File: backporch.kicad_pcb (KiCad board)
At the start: 2 copper layers, 53.3 x 32.4 mm, 31 parts, among them J1 MD-90SM, J2 MD-80SM, J3 DB15_Female_HighDensity_Mount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, J4 35RAPC4BH3, U1 EL1883ISZ

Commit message: PCB: add space between signal traces
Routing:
- net GREEN_75: track 49.7 -> 52.3 mm
- net Net-(C6-Pad1): track 39.5 -> 40.1 mm
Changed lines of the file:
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@@
     (thickness 1.6)
     (drawings 7)
-    (tracks 227)
+    (tracks 229)
     (zones 0)
     (modules 31)
@@
   (segment (start 114.935 92.51) (end 114.935 91.44) (width 0.25) (layer B.Cu) (net 8) (status 10))
   (segment (start 135.475 79.375) (end 136.525 79.375) (width 0.25) (layer F.Cu) (net 8) (status 20))
-  (segment (start 112.395 88.9) (end 112.395 83.114732) (width 0.25) (layer F.Cu) (net 8))
   (segment (start 112.395 83.114732) (end 116.519742 78.98999) (width 0.25) (layer F.Cu) (net 8))
   (segment (start 116.519742 78.98999) (end 126.240832 78.98999) (width 0.25) (layer F.Cu) (net 8))
-  (segment (start 134.349999 80.500001) (end 135.475 79.375) (width 0.25) (layer F.Cu) (net 8))
-  (segment (start 126.240832 78.98999) (end 127.750843 80.500001) (width 0.25) (layer F.Cu) (net 8))
-  (segment (start 127.750843 80.500001) (end 134.349999 80.500001) (width 0.25) (layer F.Cu) (net 8))
+  (segment (start 112.395 88.9) (end 112.395 83.114732) (width 0.25) (layer F.Cu) (net 8))
+  (segment (start 126.240832 78.98999) (end 128.530842 81.28) (width 0.25) (layer F.Cu) (net 8))
+  (segment (start 128.530842 81.28) (end 133.57 81.28) (width 0.25) (layer F.Cu) (net 8))
+  (segment (start 133.57 81.28) (end 135.475 79.375) (width 0.25) (layer F.Cu) (net 8))
   (segment (start 138.6475 79.1175) (end 138.39 79.375) (width 0.25) (layer B.Cu) (net 9) (status 30))
   (segment (start 138.865 78.9) (end 138.39 79.375) (width 0.25) (layer B.Cu) (net 9) (status 30))
   (segment (start 139.065 79.335) (end 139.025 79.375) (width 0.25) (layer B.Cu) (net 9) (status 30))
   (segment (start 139.065 77.47) (end 139.065 79.335) (width 0.25) (layer B.Cu) (net 9) (status 30))
-  (segment (start 127.779999 86.442999) (end 133.722997 80.500001) (width 0.25) (layer B.Cu) (net 9))
-  (segment (start 137.899999 80.500001) (end 139.025 79.375) (width 0.25) (layer B.Cu) (net 9) (status 20))
-  (segment (start 127.779999 88.120001) (end 127.779999 86.442999) (width 0.25) (layer B.Cu) (net 9))
-  (segment (start 125.32749 90.57251) (end 127.779999 88.120001) (width 0.25) (layer B.Cu) (net 9))
-  (segment (start 133.722997 80.500001) (end 137.899999 80.500001) (width 0.25) (layer B.Cu) (net 9))
-  (segment (start 119.4168 90.57251) (end 125.32749 90.57251) (width 0.25) (layer B.Cu) (net 9))
-  (segment (start 117.21 92.77931) (end 119.4168 90.57251) (width 0.25) (layer B.Cu) (net 9))
-  (segment (start 117.21 96.665) (end 117.21 92.77931) (width 0.25) (layer B.Cu) (net 9) (status 10))
   (segment (start 148.17363 89.655) (end 148.59 89.655) (width 0.25) (layer F.Cu) (net 9) (status 30))
   (segment (start 139.025 80.50637) (end 148.17363 89.655) (width 0.25) (layer F.Cu) (net 9) (status 20))
   (segment (start 139.025 79.375) (end 139.025 80.50637) (width 0.25) (layer F.Cu) (net 9) (status 10))
+  (segment (start 117.21 91.705) (end 117.21 96.665) (width 0.25) (layer B.Cu) (net 9) (status 20))
+  (segment (start 118.11 90.805) (end 117.21 91.705) (width 0.25) (layer B.Cu) (net 9))
+  (segment (start 126.365 85.725) (end 126.365 90.805) (width 0.25) (layer B.Cu) (net 9))
+  (segment (start 126.365 90.805) (end 118.11 90.805) (width 0.25) (layer B.Cu) (net 9))
+  (segment (start 137.899999 80.500001) (end 137.899999 80.540001) (width 0.25) (layer B.Cu) (net 9))
+  (segment (start 137.899999 80.540001) (end 135.89 82.55) (width 0.25) (layer B.Cu) (net 9))
+  (segment (start 139.025 79.375) (end 137.899999 80.500001) (width 0.25) (layer B.Cu) (net 9) (status 10))
+  (segment (start 131.445 82.55) (end 128.27 85.725) (width 0.25) (layer B.Cu) (net 9))
+  (segment (start 135.89 82.55) (end 131.445 82.55) (width 0.25) (layer B.Cu) (net 9))
+  (segment (start 128.27 85.725) (end 126.365 85.725) (width 0.25) (layer B.Cu) (net 9))
   (via (at 139.7 83.82) (size 0.8) (drill 0.4) (layers F.Cu B.Cu) (net 10))
   (via (at 127 95.25) (size 0.8) (drill 0.4) (layers F.Cu B.Cu) (net 10))

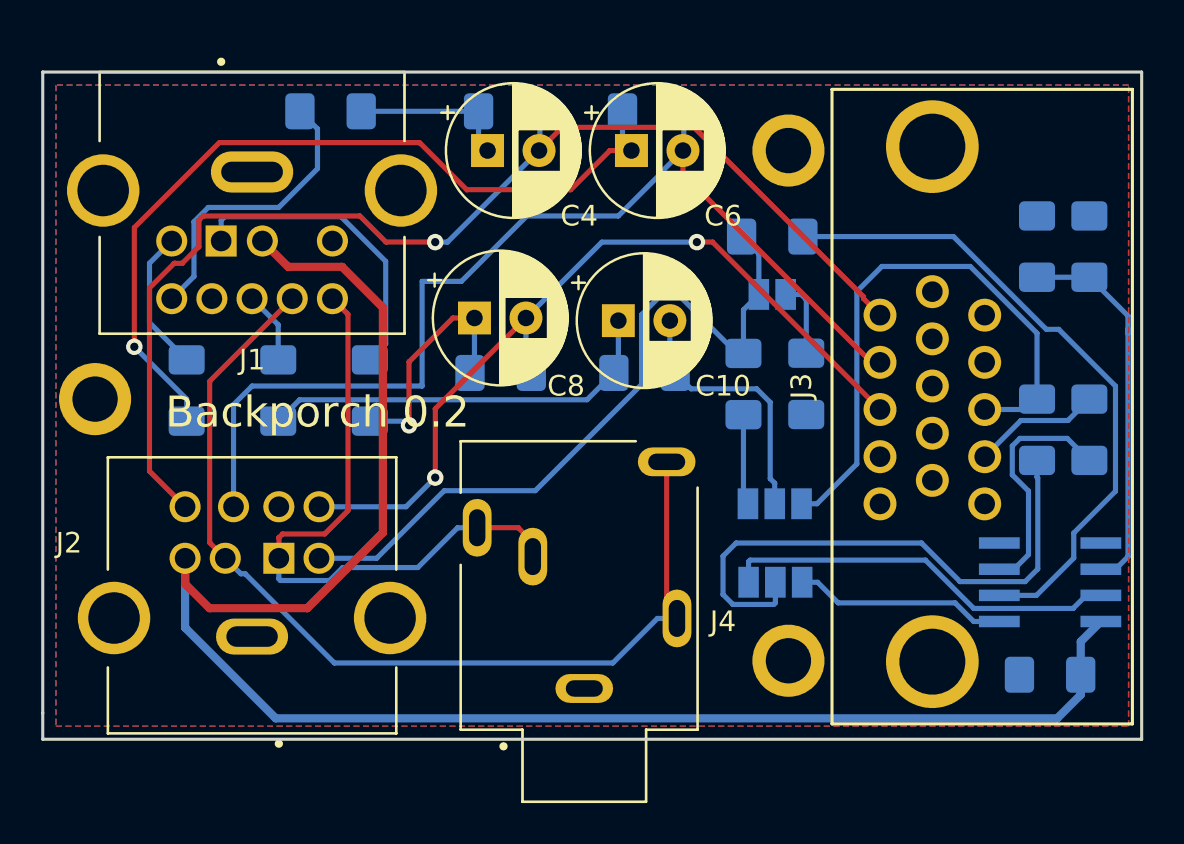
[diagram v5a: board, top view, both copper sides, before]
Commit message: Footprints: add external footprints to project
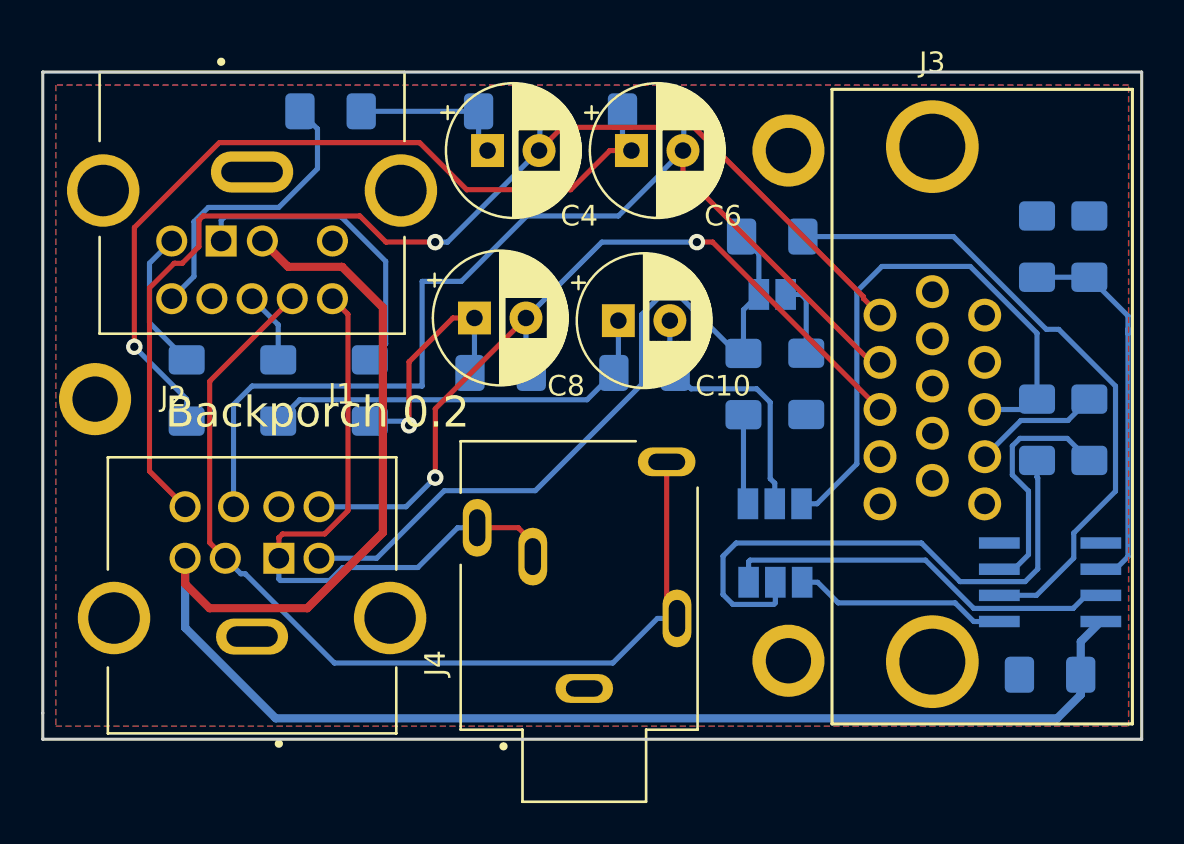
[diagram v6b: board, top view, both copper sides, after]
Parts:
- J1: footprint MD90:CUI_MD-90SM -> project-footprints:CUI_MD-90SM
- J2: footprint MD80:CUI_MD-80SM -> project-footprints:CUI_MD-80SM
- J3: footprint VGA-from-OSSC:VGA_CONN -> project-footprints:VGA_CONN
- J4: footprint 35RAPC4BH3:SWITCHCRAFT_35RAPC4BH3 -> project-footprints:SWITCHCRAFT_35RAPC4BH3
- U1: footprint EL1883ISZ:SOIC127P600X175-8N -> project-footprints:SOIC127P600X175-8N
